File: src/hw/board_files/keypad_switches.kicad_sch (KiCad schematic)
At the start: 24 parts, among them SW10 SW_Push, SW11 SW_Push, SW12 SW_Push, SW13 SW_Push, SW2 SW_Push, SW3 SW_Push, SW4 SW_Push, SW5 SW_Push, SW6 SW_Push, SW7 SW_Push, SW8 SW_Push, SW9 SW_Push

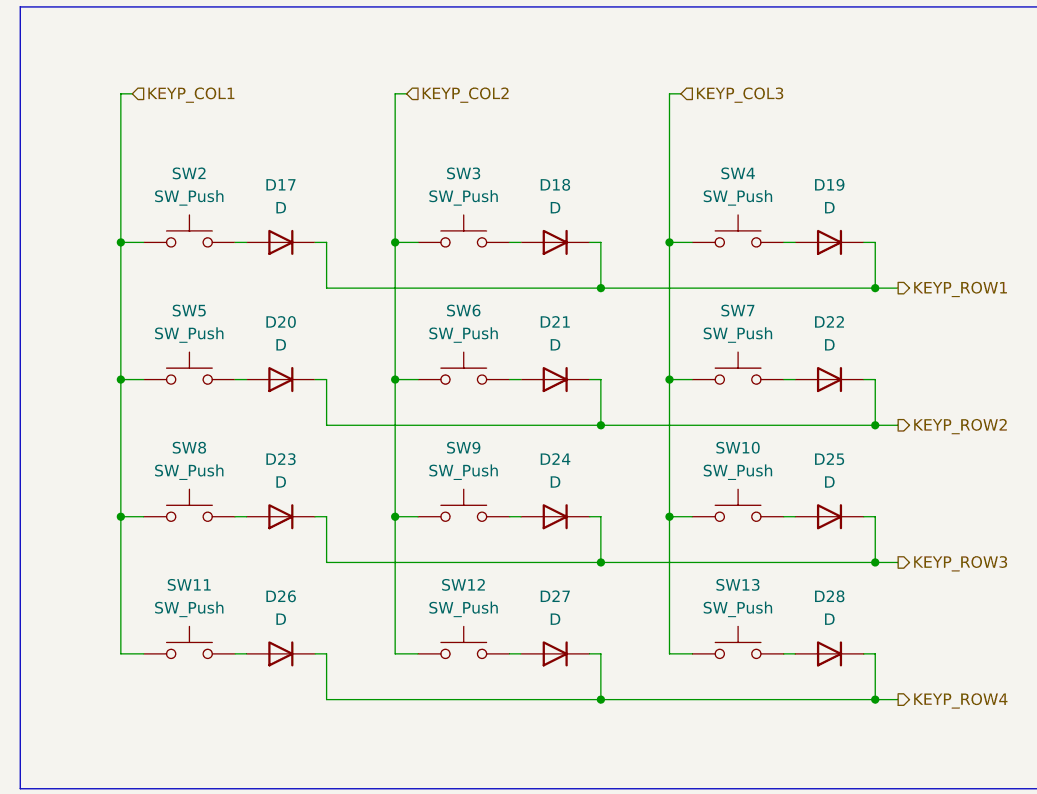
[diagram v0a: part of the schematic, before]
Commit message: Added all footprints, need to connect switches to MCU
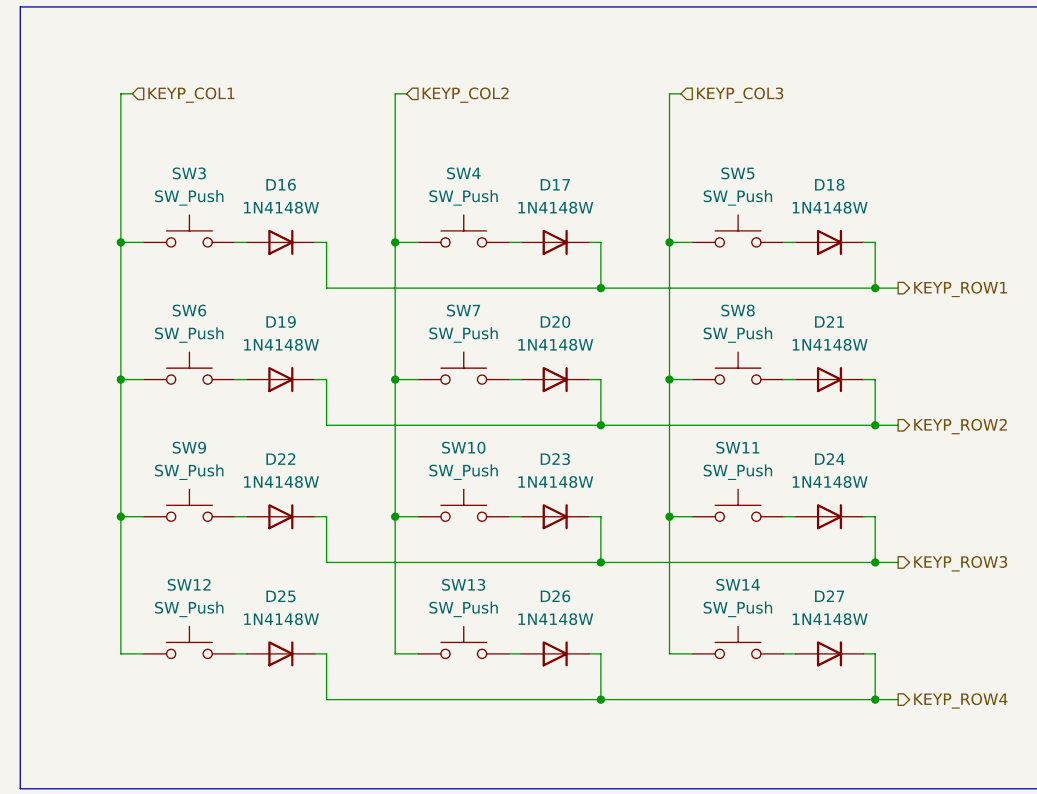
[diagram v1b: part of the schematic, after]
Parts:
- removed D17, D18, D19, D20, D21, D22, D23, D24, D25, D26, D27, D28: D, symbol Device:D
- added D16, D17, D18, D19, D20, D21, D22, D23, D24, D25, D26, D27: 1N4148W, Diode_SMD:D_SOD-123, symbol Diode:1N4148W
- SW10: renamed from SW9; footprint (none) -> Button_Switch_Keyboard:SW_Cherry_MX_1.00u_PCB
- SW11: renamed from SW10; footprint (none) -> Button_Switch_Keyboard:SW_Cherry_MX_1.00u_PCB
- SW12: renamed from SW11; footprint (none) -> Button_Switch_Keyboard:SW_Cherry_MX_1.00u_PCB
- SW13: renamed from SW12; footprint (none) -> Button_Switch_Keyboard:SW_Cherry_MX_1.00u_PCB
- SW14: renamed from SW13; footprint (none) -> Button_Switch_Keyboard:SW_Cherry_MX_1.00u_PCB
- SW3: renamed from SW2; footprint (none) -> Button_Switch_Keyboard:SW_Cherry_MX_1.00u_PCB
- SW4: renamed from SW3; footprint (none) -> Button_Switch_Keyboard:SW_Cherry_MX_1.00u_PCB
- SW5: renamed from SW4; footprint (none) -> Button_Switch_Keyboard:SW_Cherry_MX_1.00u_PCB
- SW6: renamed from SW5; footprint (none) -> Button_Switch_Keyboard:SW_Cherry_MX_1.00u_PCB
- SW7: renamed from SW6; footprint (none) -> Button_Switch_Keyboard:SW_Cherry_MX_1.00u_PCB
- SW8: renamed from SW7; footprint (none) -> Button_Switch_Keyboard:SW_Cherry_MX_1.00u_PCB
- SW9: renamed from SW8; footprint (none) -> Button_Switch_Keyboard:SW_Cherry_MX_1.00u_PCB
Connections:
- net KEYP_ROW1: now also D16.1 (K), D17.1 (K), D18.1 (K)
- net KEYP_ROW2: now also D19.1 (K), D20.1 (K), D21.1 (K)
- net KEYP_ROW3: now also D22.1 (K), D23.1 (K), D24.1 (K)
- net KEYP_ROW4: now also D25.1 (K), D26.1 (K), D27.1 (K)
- net at SW4.2: now also D17.2 (A)
- net at SW7.2: now also D20.2 (A)
- net at SW3.2: now also D16.2 (A)
- net at SW6.2: now also D19.2 (A)
- net at SW12.2: now also D25.2 (A)
- net at SW10.2: now also D23.2 (A)
- net at SW8.2: now also D21.2 (A)
- net at SW11.2: now also D24.2 (A)
- net at SW9.2: now also D22.2 (A)
- net at SW5.2: now also D18.2 (A)
- net at SW14.2: now also D27.2 (A)
- net at SW13.2: now also D26.2 (A)

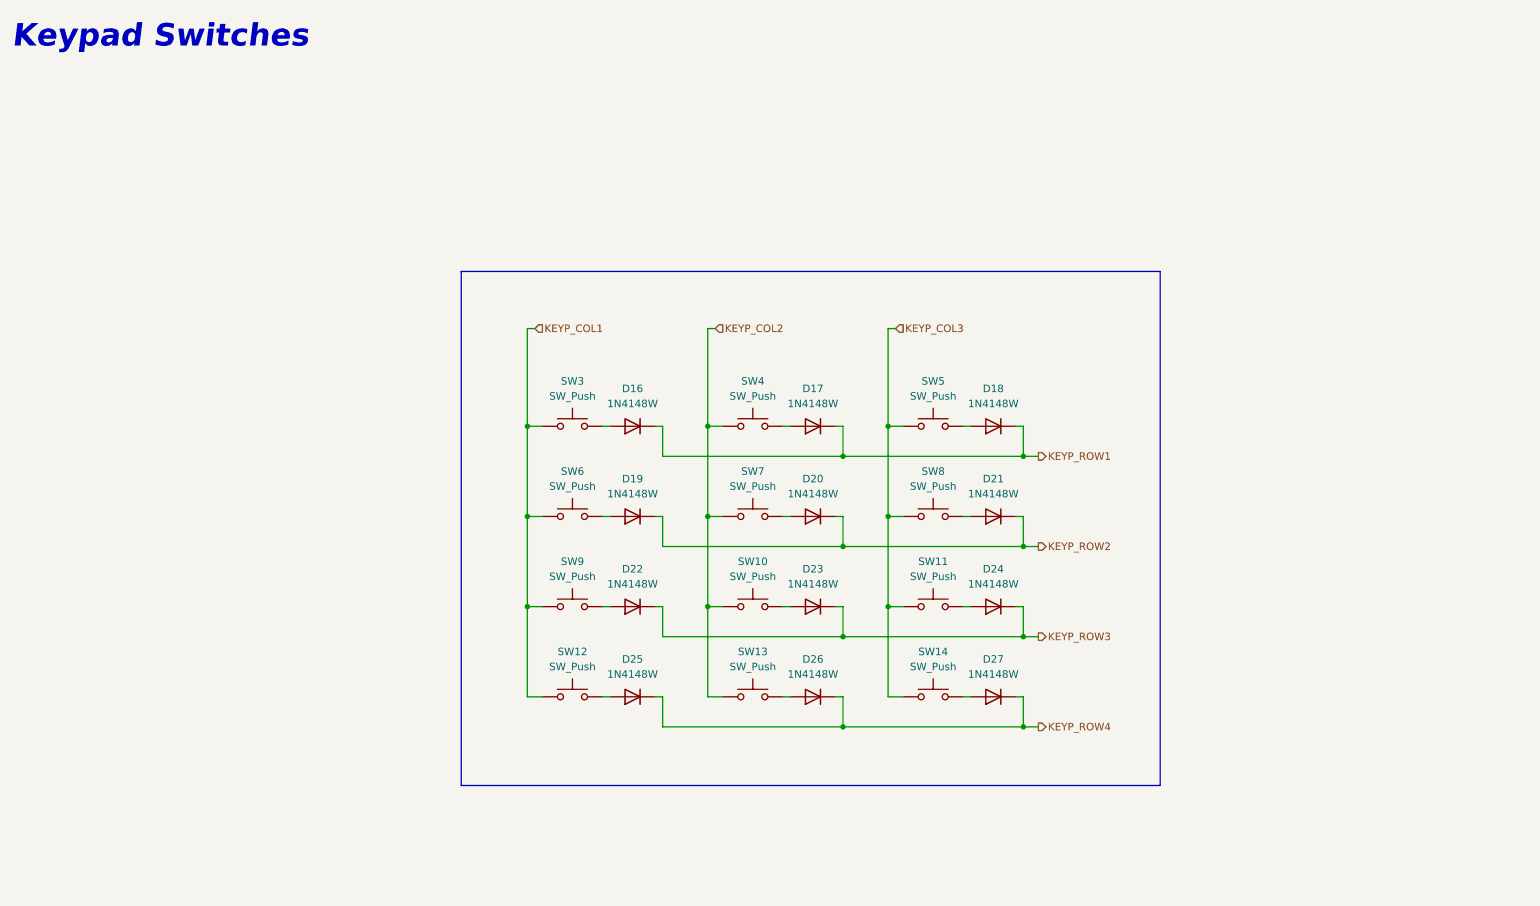
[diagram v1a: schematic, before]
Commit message: Added rotary encoder and OLED. Started laying out board then I need to review schematic and change pinout if needed
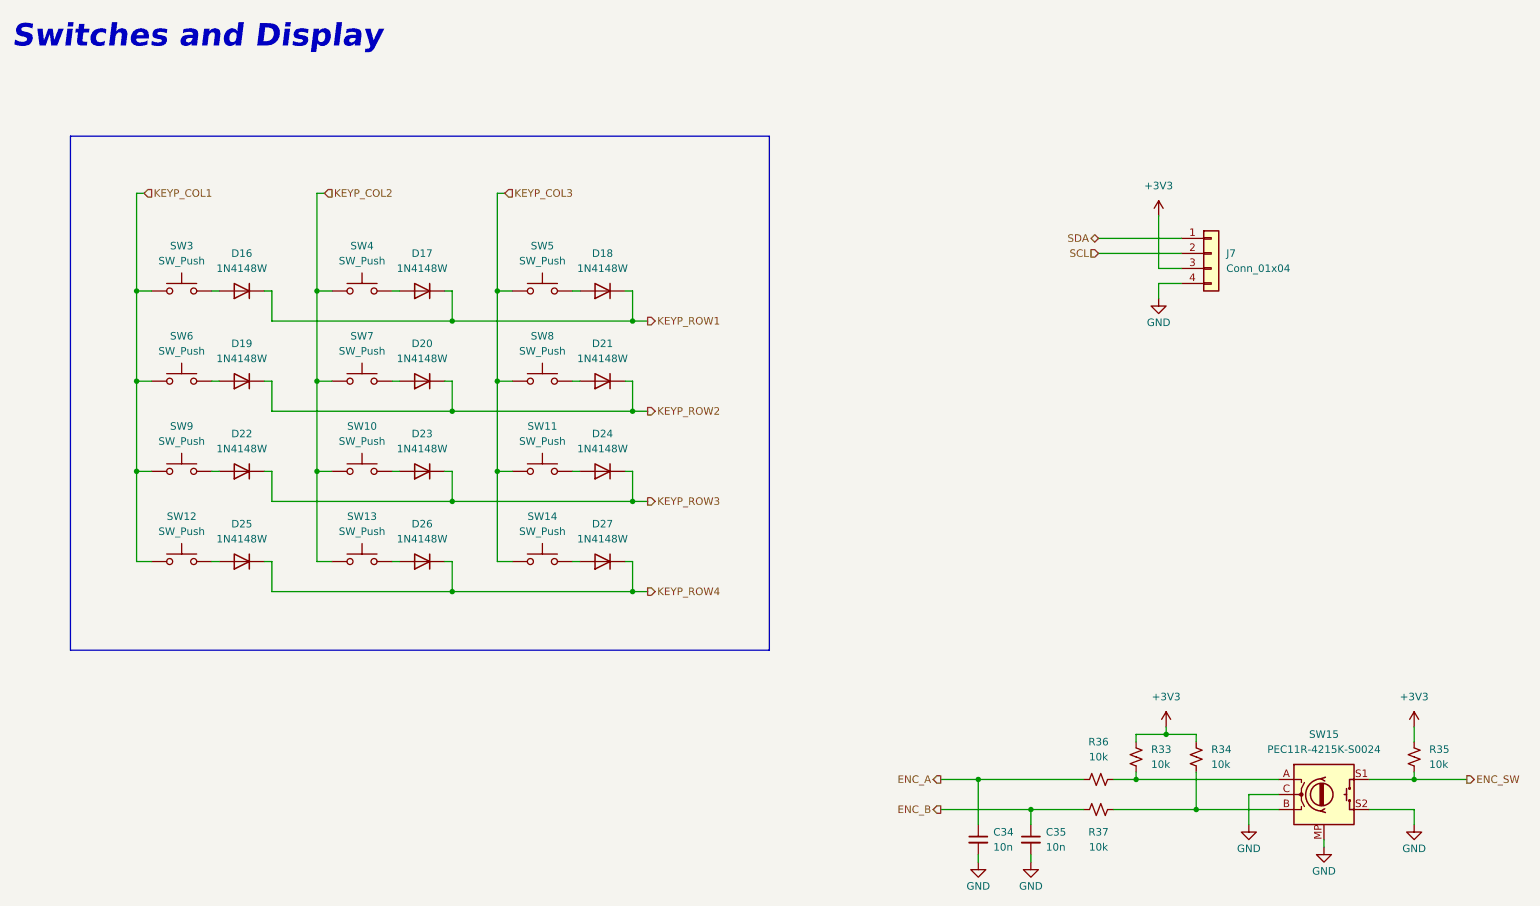
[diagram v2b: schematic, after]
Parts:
- added C34, C35: 10n, Capacitor_SMD:C_0603_1608Metric_Pad1.08x0.95mm_HandSolder, symbol Device:C_Small
- added J7: Conn_01x04, Connector_PinSocket_2.54mm:PinSocket_1x04_P2.54mm_Vertical, symbol Connector_Generic:Conn_01x04
- added R33, R34, R35, R36, R37: 10k, Resistor_SMD:R_0603_1608Metric_Pad0.98x0.95mm_HandSolder, symbol Device:R_Small_US
- added SW15: PEC11R-4215K-S0024, Rotary_Encoder:RotaryEncoder_Alps_EC12E-Switch_Vertical_H20mm, symbol Device:RotaryEncoder_Switch_MP
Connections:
- new net: R33.2, R36.2, SW15.A
- new net: R34.2, R37.2, SW15.B
- new net +3V3: J7.3 (Pin_3), R33.1, R34.1, R35.1
- new net ENC_A: C34.1, R36.1
- new net ENC_B: C35.1, R37.1
- new net ENC_SW: R35.2, SW15.S1
- new net GND: C34.2, C35.2, J7.4 (Pin_4), SW15.C, SW15.MP, SW15.S2
- new net SCL: J7.2 (Pin_2)
- new net SDA: J7.1 (Pin_1)
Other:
- note added: "Switches and Display"
- note removed: "Keypad Switches"
- moved on the sheet: D16, D17, D18, D19, D20, D21, D22, D23, D24, D25, D26, D27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
